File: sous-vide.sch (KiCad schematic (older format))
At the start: 26 parts, among them J1 Conn_01x02, J2 Conn_01x02, J3 Conn_01x02, J4 Jumper, J5 Jumper, Q1 2N3904, SW1 SW_Push_Dual, SW2 SW_Push_Dual, U1 G5LE, U2 RAC01, U3 node_mcu1.0, U4 P090S, U5 LCD_Backpack

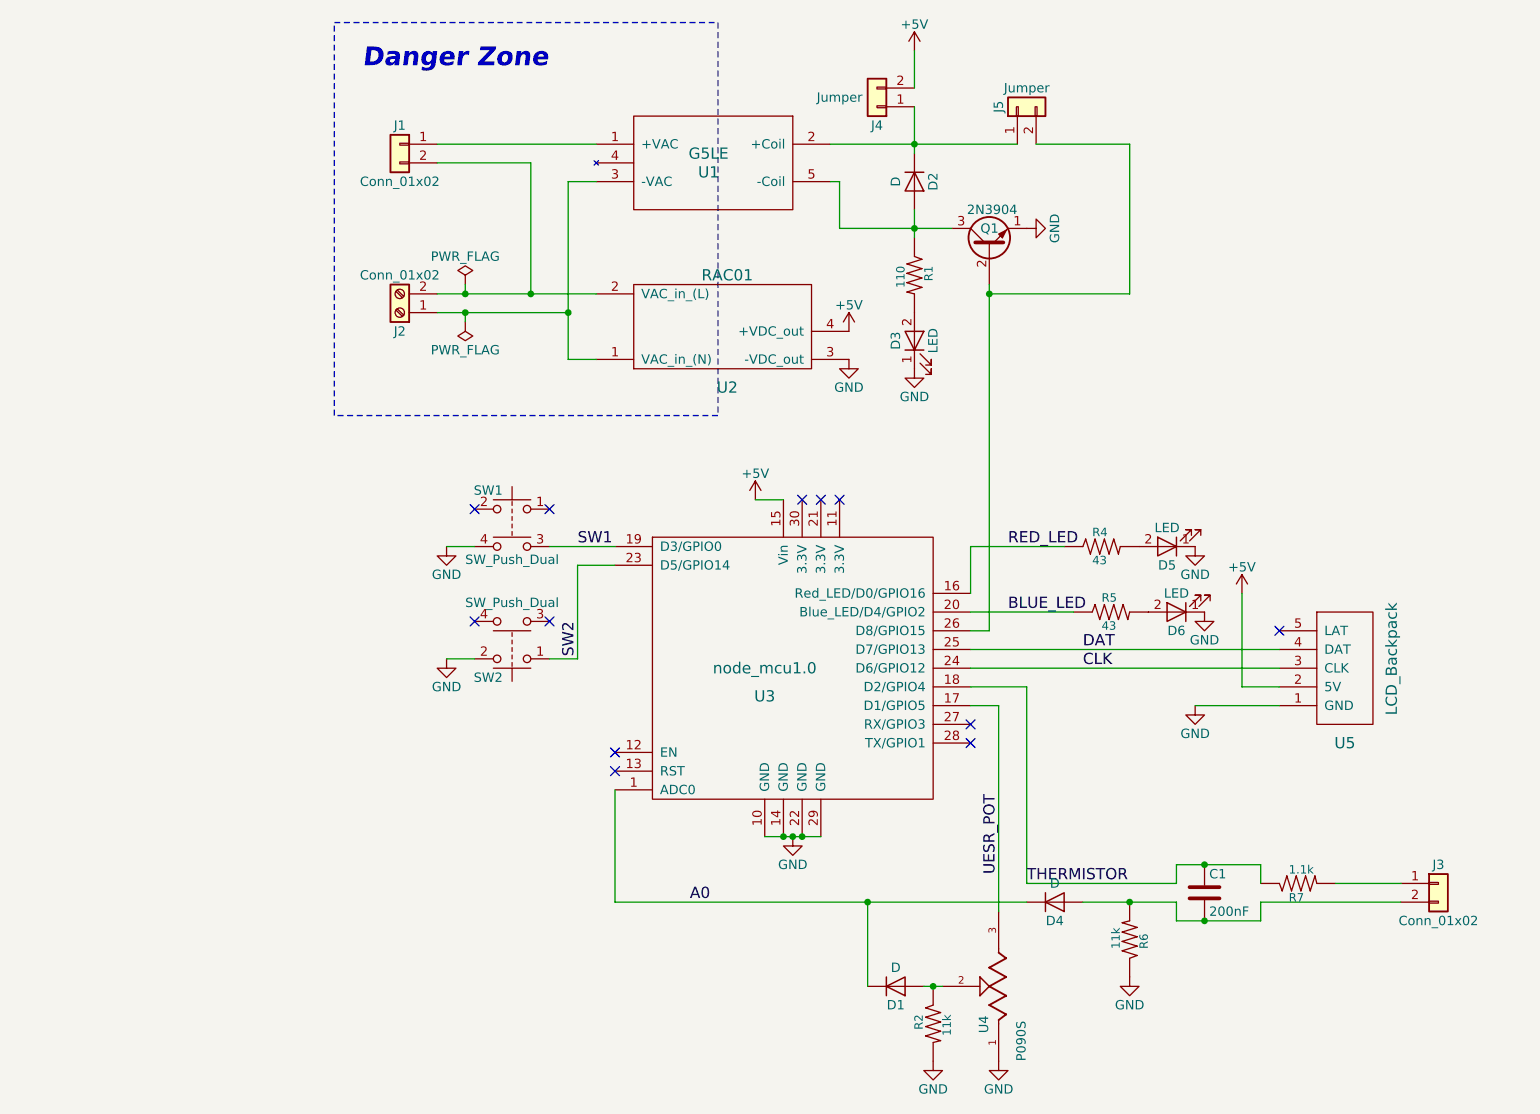
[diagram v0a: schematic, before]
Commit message: V 0.3
 - added protection circuit and fuse
 - fixed LED indicator on relay circuit with Jeff's help
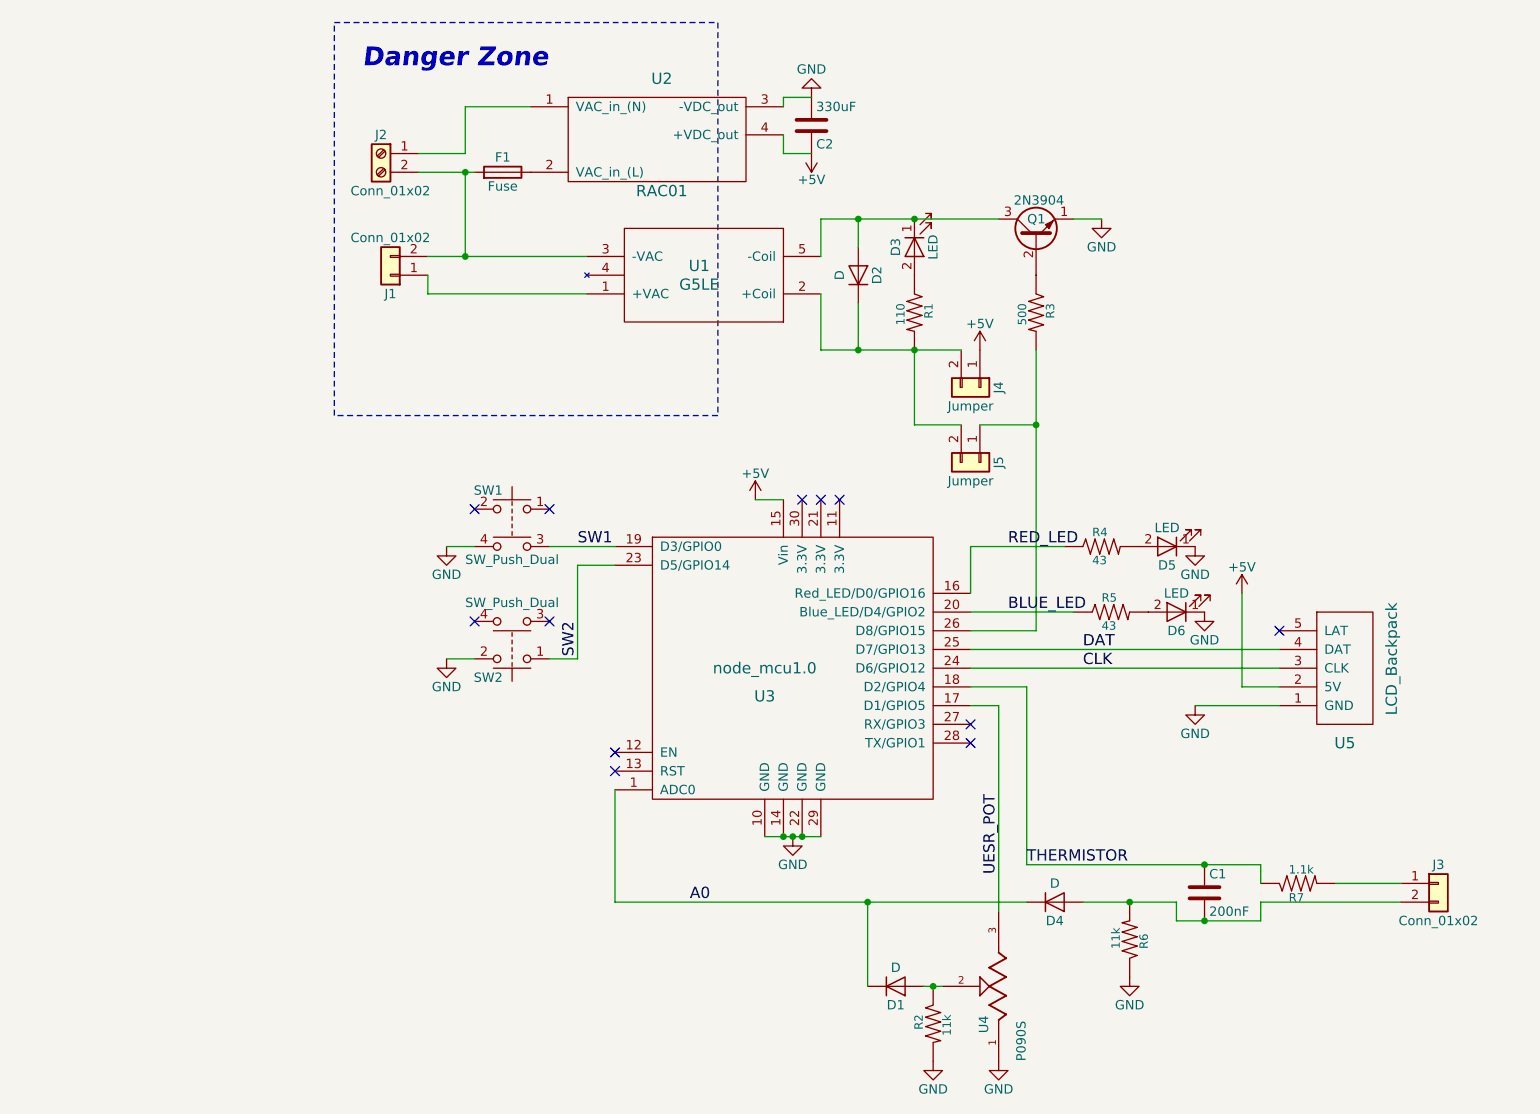
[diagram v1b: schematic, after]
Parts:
- added C2: 330uF, Capacitors_THT:CP_Radial_D8.0mm_P3.50mm, symbol C
- added F1: Fuse, custom:Fuse_Holder_65600001009, symbol Fuse
- added R3: 500, Resistors_THT:R_Axial_DIN0207_L6.3mm_D2.5mm_P10.16mm_Horizontal, symbol RESISTOR0402
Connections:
- net +5V: now also J4.1 (Pin_1), C2.1; no longer J4.2 (Pin_2)
- net GND: now also C2.2; no longer D3.1 (K)
- net at D2.2 (A), Q1.3 (C), U1.5 (-Coil): now also D3.1 (K); no longer R1.1
- net at J2.1 (Pin_1), U2.1 (VAC_in_(N)): no longer U1.3 (-VAC)
- net at J1.2 (Pin_2), J2.2 (Pin_2): now also U1.3 (-VAC), F1.2; no longer U2.2 (VAC_in_(L))
- net at D2.1 (K), U1.2 (+Coil): now also J4.2 (Pin_2), J5.2 (Pin_2), R1.2; no longer J4.1 (Pin_1), J5.1 (Pin_1)
- net at D3.2 (A): now also R1.1; no longer R1.2
- new net: Q1.2 (B), R3.1
- new net: F1.1, U2.2 (VAC_in_(L))
- new net: J5.1 (Pin_1), R3.2, U3.26 (D8/GPIO15)
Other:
- moved on the sheet: D2, D3, J1, J2, J4, J5, Q1, R1, U1, U2

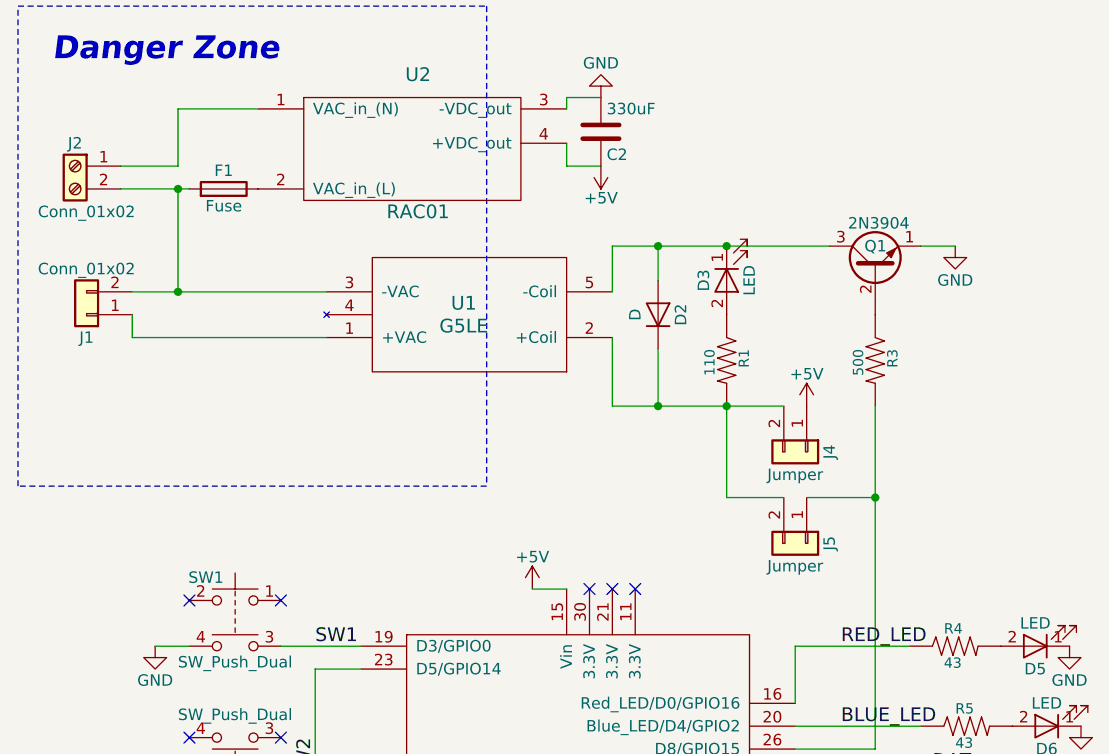
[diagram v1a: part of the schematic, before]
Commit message: fix power circuit
 - reroute
 - make board slightly bigger
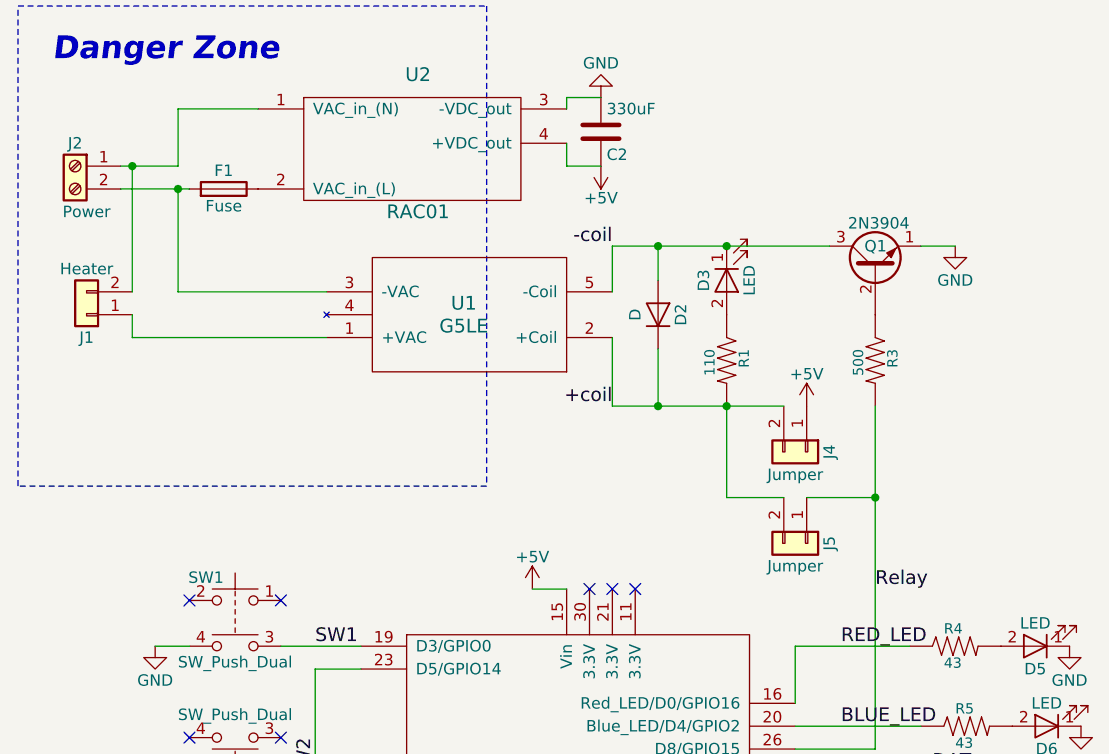
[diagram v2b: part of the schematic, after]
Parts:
- J1: value Conn_01x02 -> Heater
- J2: value Conn_01x02 -> Power
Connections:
- net -coil: now reaches D2.2 (A), D3.1 (K), Q1.3 (C), U1.5 (-Coil)
- net at J2.1 (Pin_1), U2.1 (VAC_in_(N)): now also J1.2 (Pin_2)
- net +coil: now reaches D2.1 (K), J4.2 (Pin_2), J5.2 (Pin_2), R1.2, U1.2 (+Coil)
- net at F1.2, J2.2 (Pin_2), U1.3 (-VAC): no longer J1.2 (Pin_2)
- net Relay: now reaches J5.1 (Pin_1), R3.2, U3.26 (D8/GPIO15)
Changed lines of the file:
@@
 P 3200 1450
 F 0 "J2" H 3200 1550 50  0000 C CNN
-F 1 "Conn_01x02" H 3150 1250 50  0000 C CNN
+F 1 "Power" H 3150 1250 50  0000 C CNN
 F 2 "custom:NC6-P108-02" H 3200 1450 50  0001 C CNN
 F 3 "" H 3200 1450 50  0001 C CNN
@@
 P 3250 2100
 F 0 "J1" H 3250 2200 50  0000 C CNN
-F 1 "Conn_01x02" H 3250 1900 50  0000 C CNN
+F 1 "Heater" H 3250 1900 50  0000 C CNN
 F 2 "custom:NC6-P108-02" H 3250 2100 50  0001 C CNN
 F 3 "" H 3250 2100 50  0001 C CNN
@@
 	0    1    1    0
 $EndComp
-Wire Wire Line
-	6950 5450 7450 5450
-Connection ~ 7200 5450
-Wire Wire Line
-	6100 5900 6200 5900
-Wire Wire Line
-	3550 3550 3700 3550
-Wire Wire Line
-	3550 4150 3700 4150
-Wire Wire Line
-	4100 3550 4450 3550
-Wire Wire Line
-	6350 3550 6350 3800
-Wire Wire Line
-	7800 4300 8000 4300
-Wire Wire Line
-	8000 4400 7550 4400
-Wire Wire Line
-	6350 3550 6850 3550
-Wire Wire Line
-	6900 3900 6350 3900
-Wire Wire Line
-	6500 4400 6500 5500
-Wire Wire Line
-	7800 3800 7800 4300
-Wire Wire Line
-	5200 3300 5350 3300
-Wire Wire Line
-	6650 4300 6650 5250
-Connection ~ 6150 5900
-Wire Wire Line
-	4450 5450 6650 5450
-Wire Wire Line
-	4450 5450 4450 4850
-Wire Wire Line
-	5800 5900 5800 5450
-Connection ~ 5800 5450
-Wire Notes Line
-	2950 2850 2950 750
-Wire Notes Line
-	2950 750  5000 750
-Wire Notes Line
-	5000 2850 2950 2850
-Wire Wire Line
-	6500 4400 6350 4400
-Wire Wire Line
-	6650 4300 6350 4300
-Wire Wire Line
-	6350 4200 8000 4200
-Wire Wire Line
-	6350 4100 8000 4100
-Wire Wire Line
-	6700 4000 6350 4000
-Wire Wire Line
-	3400 1450 3650 1450
-Wire Wire Line
-	3450 2000 4300 2000
-Wire Wire Line
-	5250 5100 5550 5100
-Connection ~ 5350 5100
-Connection ~ 5400 5100
-Connection ~ 5450 5100
-Wire Wire Line
-	4100 4150 4250 4150
-Wire Wire Line
-	4250 4150 4250 3650
-Wire Wire Line
-	4250 3650 4450 3650
-Wire Wire Line
-	6650 5250 7900 5250
-Wire Wire Line
-	7900 5250 7900 5350
-Wire Wire Line
-	7450 5550 7900 5550
-Wire Wire Line
-	7900 5550 7900 5450
-Wire Wire Line
-	7450 5450 7450 5550
-Connection ~ 7600 5550
-Wire Wire Line
-	7450 5250 7450 5250
-Connection ~ 7600 5250
-Wire Wire Line
-	7900 5450 8650 5450
-Wire Wire Line
-	8300 5350 8650 5350
-Wire Wire Line
-	5750 2250 5750 2500
-Wire Wire Line
-	5550 2500 6300 2500
-Connection ~ 6050 2500
-Wire Wire Line
-	5750 1800 5750 1950
-Connection ~ 6050 1800
-Connection ~ 5750 2500
-Connection ~ 5750 1800
-Wire Wire Line
-	6900 1800 7050 1800
 $Comp
 L Fuse F1
@@
 	1    0    0    1
 $EndComp
-Wire Wire Line
-	5500 1450 5350 1450
-Wire Wire Line
-	5350 1450 5350 1350
-Wire Wire Line
-	5500 1150 5350 1150
-Wire Wire Line
-	5350 1150 5350 1200
-Wire Wire Line
-	3400 1550 3700 1550
-Wire Wire Line
-	4300 2200 3450 2200
-Wire Wire Line
-	3450 2200 3450 2100
-Wire Wire Line
-	3650 2000 3650 1550
-Connection ~ 3650 1550
-Connection ~ 3650 2000
 $Comp
 L RESISTOR0402 R3
@@
 	0    1    1    0
 $EndComp
+Text Label 6700 3300 0    60   ~ 0
+Relay
+Text Label 5550 2500 2    60   ~ 0
++coil
+Text Label 5550 1800 2    60   ~ 0
+-coil
+Wire Wire Line
+	6950 5450 7450 5450
+Connection ~ 7200 5450
+Wire Wire Line
+	6100 5900 6200 5900
+Wire Wire Line
+	3550 3550 3700 3550
+Wire Wire Line
+	3550 4150 3700 4150
+Wire Wire Line
+	4100 3550 4450 3550
+Wire Wire Line
+	6350 3550 6350 3800
+Wire Wire Line
+	7800 4300 8000 4300
+Wire Wire Line
+	8000 4400 7550 4400
+Wire Wire Line
+	6350 3550 6850 3550
+Wire Wire Line
+	6900 3900 6350 3900
+Wire Wire Line
+	6500 4400 6500 5500
+Wire Wire Line
+	7800 3800 7800 4300
+Wire Wire Line
+	5200 3300 5350 3300
+Wire Wire Line
+	6650 4300 6650 5250
+Connection ~ 6150 5900
+Wire Wire Line
+	4450 5450 6650 5450
+Wire Wire Line
+	4450 5450 4450 4850
+Wire Wire Line
+	5800 5900 5800 5450
+Connection ~ 5800 5450
+Wire Notes Line
+	2950 2850 2950 750
+Wire Notes Line
+	2950 750  5000 750
+Wire Notes Line
+	5000 2850 2950 2850
+Wire Wire Line
+	6500 4400 6350 4400
+Wire Wire Line
+	6650 4300 6350 4300
+Wire Wire Line
+	6350 4200 8000 4200
+Wire Wire Line
+	6350 4100 8000 4100
+Wire Wire Line
+	6700 4000 6350 4000
+Wire Wire Line
+	3400 1450 3650 1450
+Wire Wire Line
+	5250 5100 5550 5100
+Connection ~ 5350 5100
+Connection ~ 5400 5100
+Connection ~ 5450 5100
+Wire Wire Line
+	4100 4150 4250 4150
+Wire Wire Line
+	4250 4150 4250 3650
+Wire Wire Line
+	4250 3650 4450 3650
+Wire Wire Line
+	6650 5250 7900 5250
+Wire Wire Line
+	7900 5250 7900 5350
+Wire Wire Line
+	7450 5550 7900 5550
+Wire Wire Line
+	7900 5550 7900 5450
+Wire Wire Line
+	7450 5450 7450 5550
+Connection ~ 7600 5550
+Wire Wire Line
+	7450 5250 7450 5250
+Connection ~ 7600 5250
+Wire Wire Line
+	7900 5450 8650 5450
+Wire Wire Line
+	8300 5350 8650 5350
+Wire Wire Line
+	5750 2250 5750 2500
+Wire Wire Line
+	5550 2500 6300 2500
+Connection ~ 6050 2500
+Wire Wire Line
+	5750 1800 5750 1950
+Connection ~ 6050 1800
+Connection ~ 5750 2500
+Connection ~ 5750 1800
+Wire Wire Line
+	6900 1800 7050 1800
+Wire Wire Line
+	5500 1450 5350 1450
+Wire Wire Line
+	5350 1450 5350 1350
+Wire Wire Line
+	5500 1150 5350 1150
+Wire Wire Line
+	5350 1150 5350 1200
+Wire Wire Line
+	3400 1550 3700 1550
+Wire Wire Line
+	4300 2200 3450 2200
+Wire Wire Line
+	3450 2200 3450 2100
 Wire Wire Line
 	5550 1800 5550 2000
@@
 Wire Wire Line
 	3650 1200 4000 1200
+Connection ~ 3650 1550
+Wire Wire Line
+	4300 2000 3650 2000
+Wire Wire Line
+	3650 2000 3650 1550
+Wire Wire Line
+	3450 2000 3450 1450
+Connection ~ 3450 1450
 $EndSCHEMATC

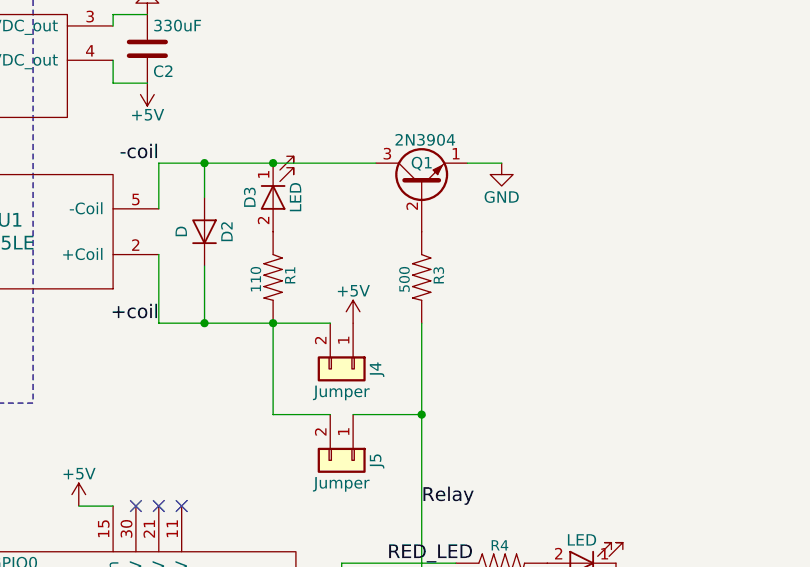
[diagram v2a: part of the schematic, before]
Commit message: breadboarded everything I could and tested
 - did not test I2C or Power Supply
 - relay state effects analog readings. bad!
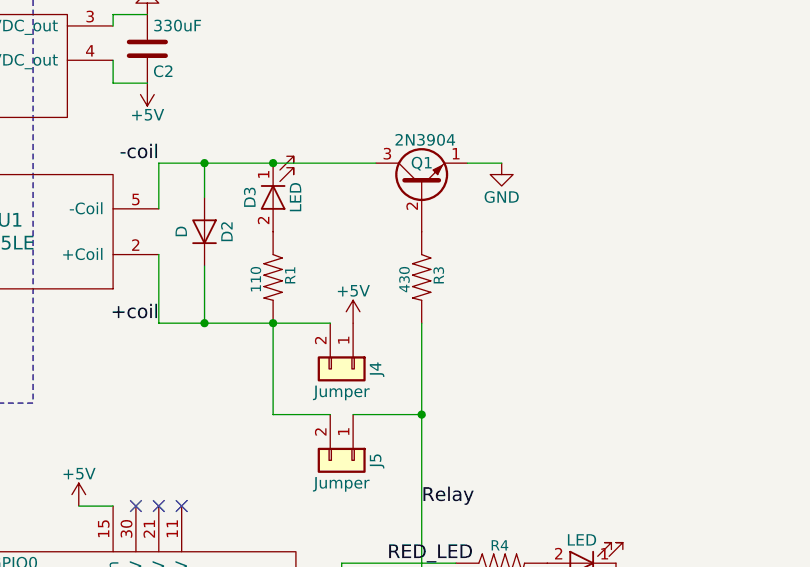
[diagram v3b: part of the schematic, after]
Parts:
- R3: value 500 -> 430
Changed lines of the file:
@@
 P 6700 2300
 F 0 "R3" H 6650 2350 45  0000 L BNN
-F 1 "500" H 6650 2200 45  0000 L BNN
+F 1 "430" H 6650 2200 45  0000 L BNN
 F 2 "Resistors_THT:R_Axial_DIN0207_L6.3mm_D2.5mm_P10.16mm_Horizontal" H 6700 2450 20  0001 C CNN
 F 3 "" H 6700 2300 60  0001 C CNN
